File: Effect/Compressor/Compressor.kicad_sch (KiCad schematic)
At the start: 49 parts, among them J1 Conn_01x04_Pin, J2 Conn_01x04_Pin, Q1 DMMT5551, Q2 MMBF5103, Q3 DMMT5551, Q4 MMBF5103

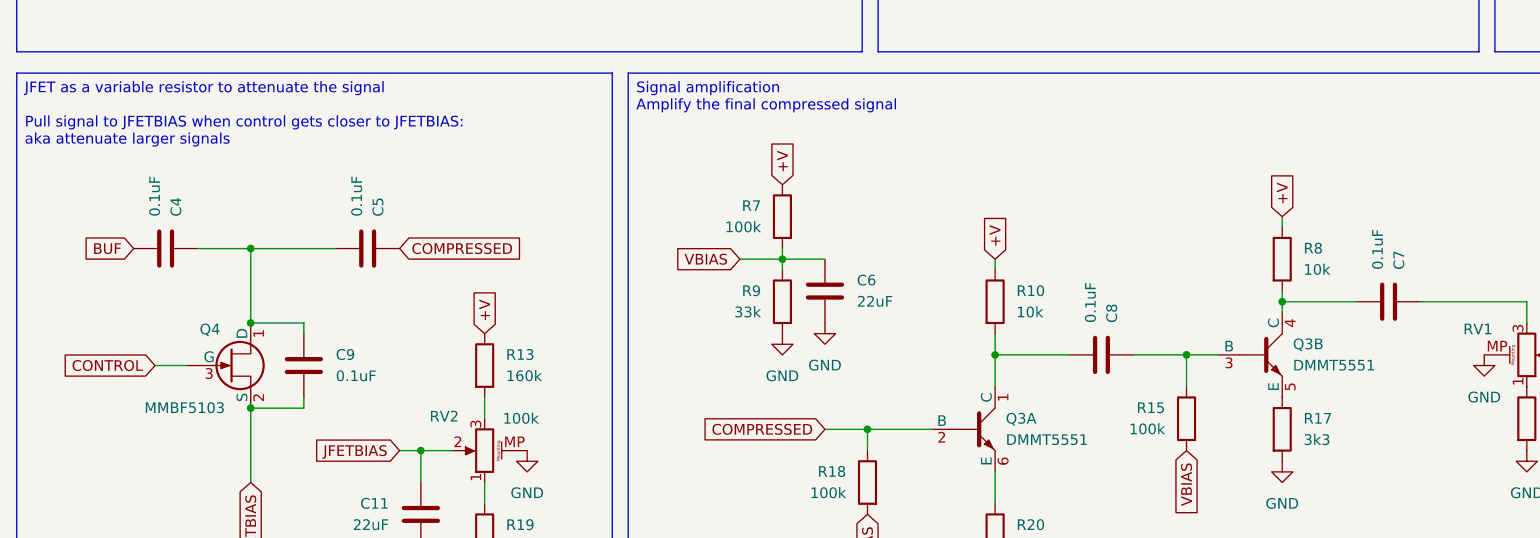
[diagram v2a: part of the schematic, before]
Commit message: Compressor: Use bigger capacitors in signal path
This just changes the 0.1uF caps in the signal path to 0.47uF ones.
That doesn't fix all ills, but it should pass lower frequency signals a
bit better.

This does make them 1206 footprints, and maybe the board will be a bit
tight.  I'm starting to look at the PCB next.

Signed-off-by: Linus Torvalds <torvalds@linux-foundation.org>
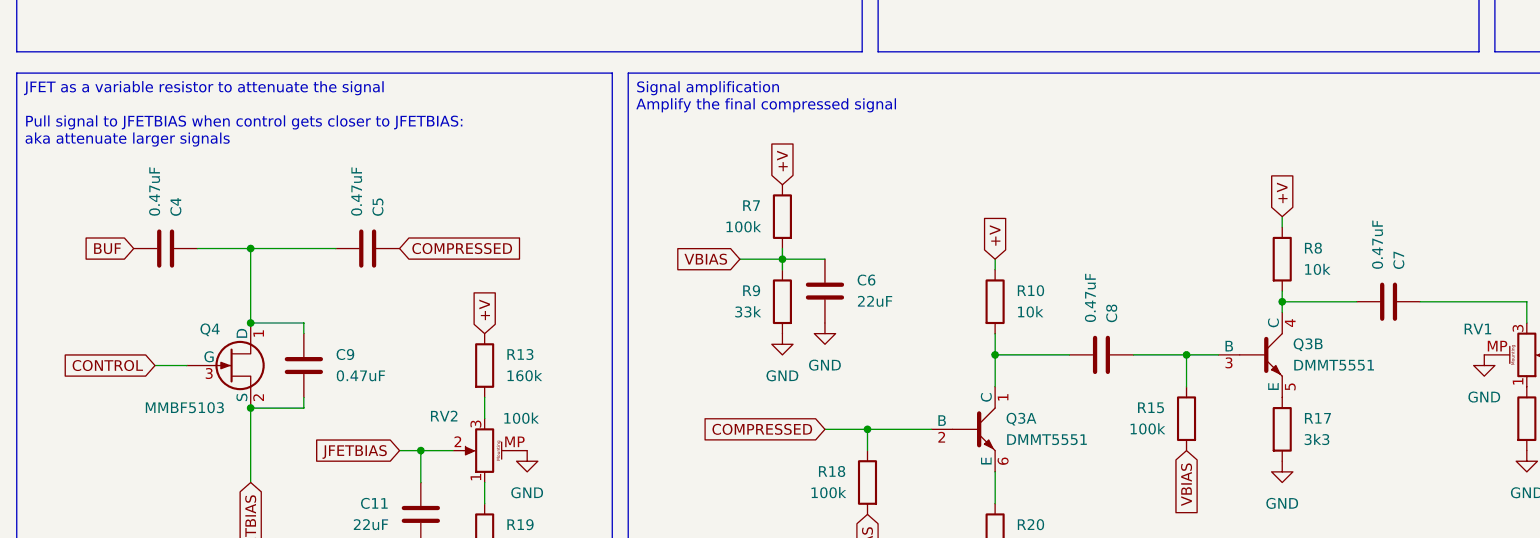
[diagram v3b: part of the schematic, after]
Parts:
- C4, C5, C7, C8, C9: value 0.1uF -> 0.47uF; footprint Mylib:C_0704_1810Metric -> Capacitor_SMD:C_1206_3216Metric
- V4: now left out of the parts list
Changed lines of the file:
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@@
 			)
 		)
-		(property "Value" "0.1uF"
+		(property "Value" "0.47uF"
 			(at 54.6101 90.17 0)
 			(effects
@@
 			)
 		)
-		(property "Footprint" "Mylib:C_0704_1810Metric"
+		(property "Footprint" "Capacitor_SMD:C_1206_3216Metric"
 			(at 52.07 93.0148 0)
 			(hide yes)
@@
 			)
 		)
-		(property "Value" "0.1uF"
+		(property "Value" "0.47uF"
 			(at 142.2401 102.87 0)
 			(effects
@@
 			)
 		)
-		(property "Footprint" "Mylib:C_0704_1810Metric"
+		(property "Footprint" "Capacitor_SMD:C_1206_3216Metric"
 			(at 139.7 105.7148 0)
 			(hide yes)
@@
 			)
 		)
-		(property "Value" "0.1uF"
+		(property "Value" "0.47uF"
 			(at 52.07 109.2199 0)
 			(effects
@@
 			)
 		)
-		(property "Footprint" "Mylib:C_0704_1810Metric"
+		(property "Footprint" "Capacitor_SMD:C_1206_3216Metric"
 			(at 49.2252 111.76 0)
 			(hide yes)
@@
 			)
 		)
-		(property "Value" "0.1uF"
+		(property "Value" "0.47uF"
 			(at 176.5301 96.52 0)
 			(effects
@@
 			)
 		)
-		(property "Footprint" "Mylib:C_0704_1810Metric"
+		(property "Footprint" "Capacitor_SMD:C_1206_3216Metric"
 			(at 173.99 99.3648 0)
 			(hide yes)
@@
 		(unit 1)
 		(exclude_from_sim no)
-		(in_bom yes)
-		(on_board yes)
+		(in_bom no)
+		(on_board no)
 		(dnp no)
 		(fields_autoplaced yes)
@@
 			)
 		)
-		(property "Value" "0.1uF"
+		(property "Value" "0.47uF"
 			(at 30.4801 90.17 0)
 			(effects
@@
 			)
 		)
-		(property "Footprint" "Mylib:C_0704_1810Metric"
+		(property "Footprint" "Capacitor_SMD:C_1206_3216Metric"
 			(at 27.94 93.0148 0)
 			(hide yes)

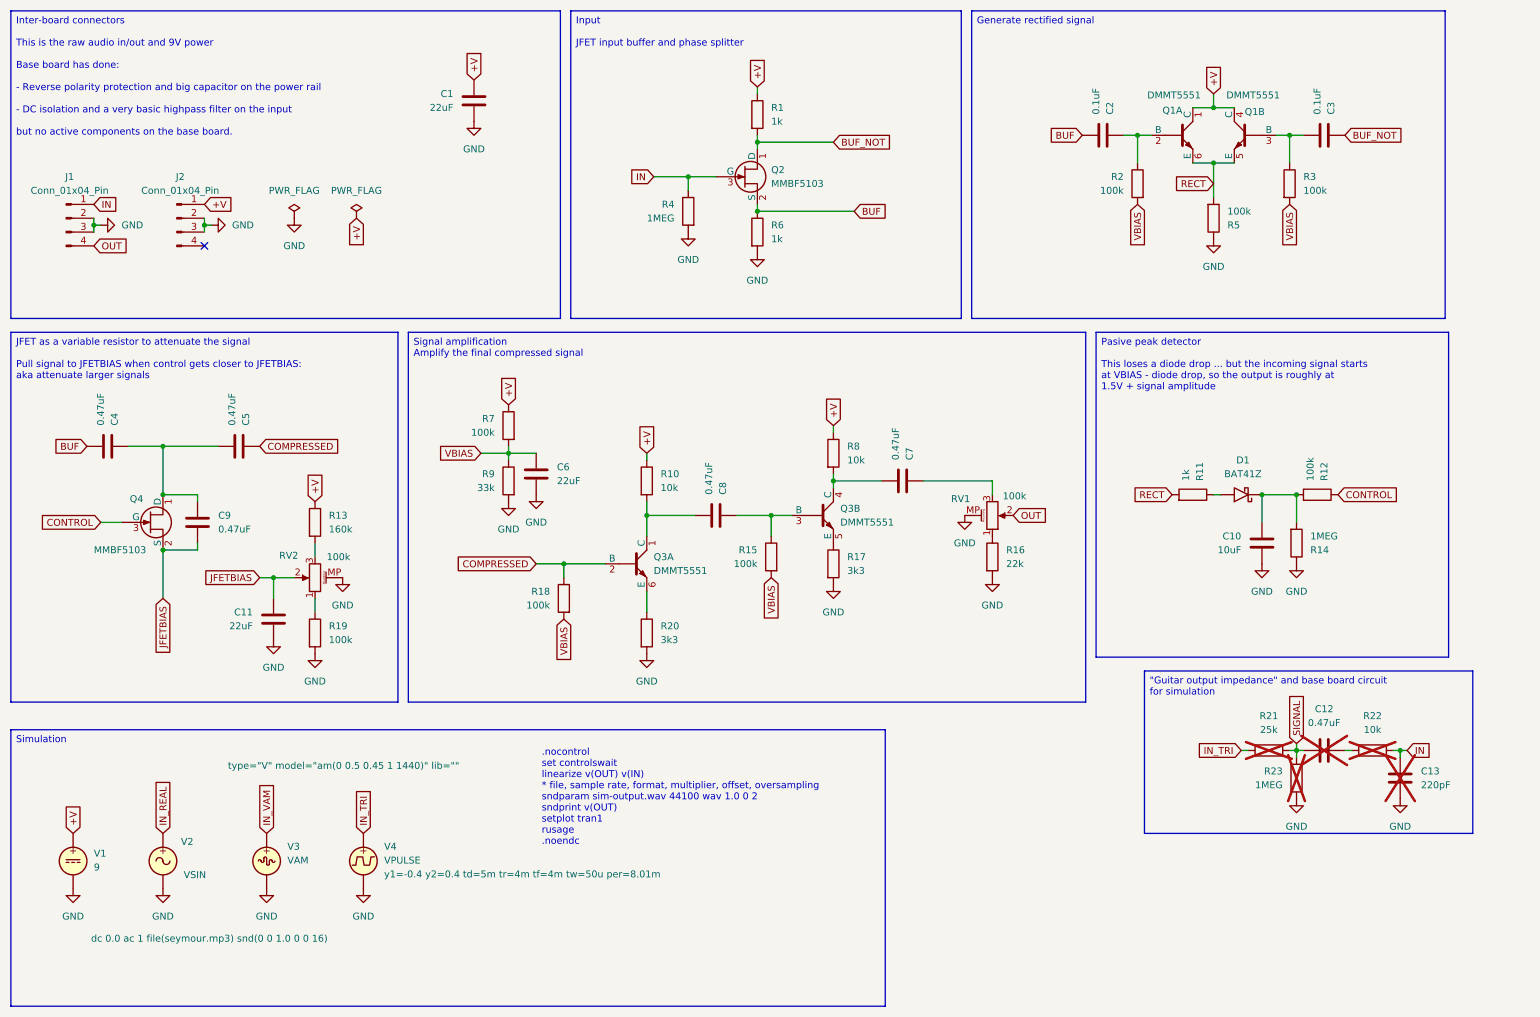
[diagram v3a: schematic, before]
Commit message: Compressor: re-do with feedback loop and a whole new approach
So as mentioned earlier I started looking into using a feedback loop
rather than base the compression purely on the input signal amplitude,
and as I was working on that, I realized that I had been thinking of the
JFET signal attenuation entirely the wrong way the whole time.

My confusion actually started way back with the old tremolo circuit that
I had so many problems with, and it all stems from just thinking that I
should use the JFET as a variable resistor to pull the signal down to
ground.

Yeah, yeah, that makes conceptual sense, but it's actually not the right
way to go about this all, because I realized that I was just making
things much harder than they needed to be.

It's much simpler and more practical to use a regular fixed resistor to
attenuate the signal by pulling it down to ground, and use the JFET to
actually _pass_ the signal.  After all, the default for the JFET is to
conduct, and R_{DS(ON)} is some reasonably small value like 50 Ohm.

So just turn things around, and it all becomes much more natural: with a
regular pull-down resistor in the kOhm range, the "normal" situation
(the JFET gate not actively pulled down) being that the JFET conducts
the signal and there is little to no attenuation.

Then when we want to attenuate the signal, we pull the gate down, and it
turns out that there's a very natural way to generate a negative signal
even without a dual power rail: just amplify the signal to have a large
enough voltage swing, and then do just a "voltage doubler" with two
capacitors and diodes.

It's just an inverting charge pump on the signal, in other words.  And
since it goes to the gate of the JFET, there's no need for any current.

Ta-daa, you have a nice negative voltage matching the signal amplitude
(with two diode drops, but just use a low-drop Schottky to minimize that
too).

And now the "add in half the input signal to the control signal" that I
had seen mentioned in JFET com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
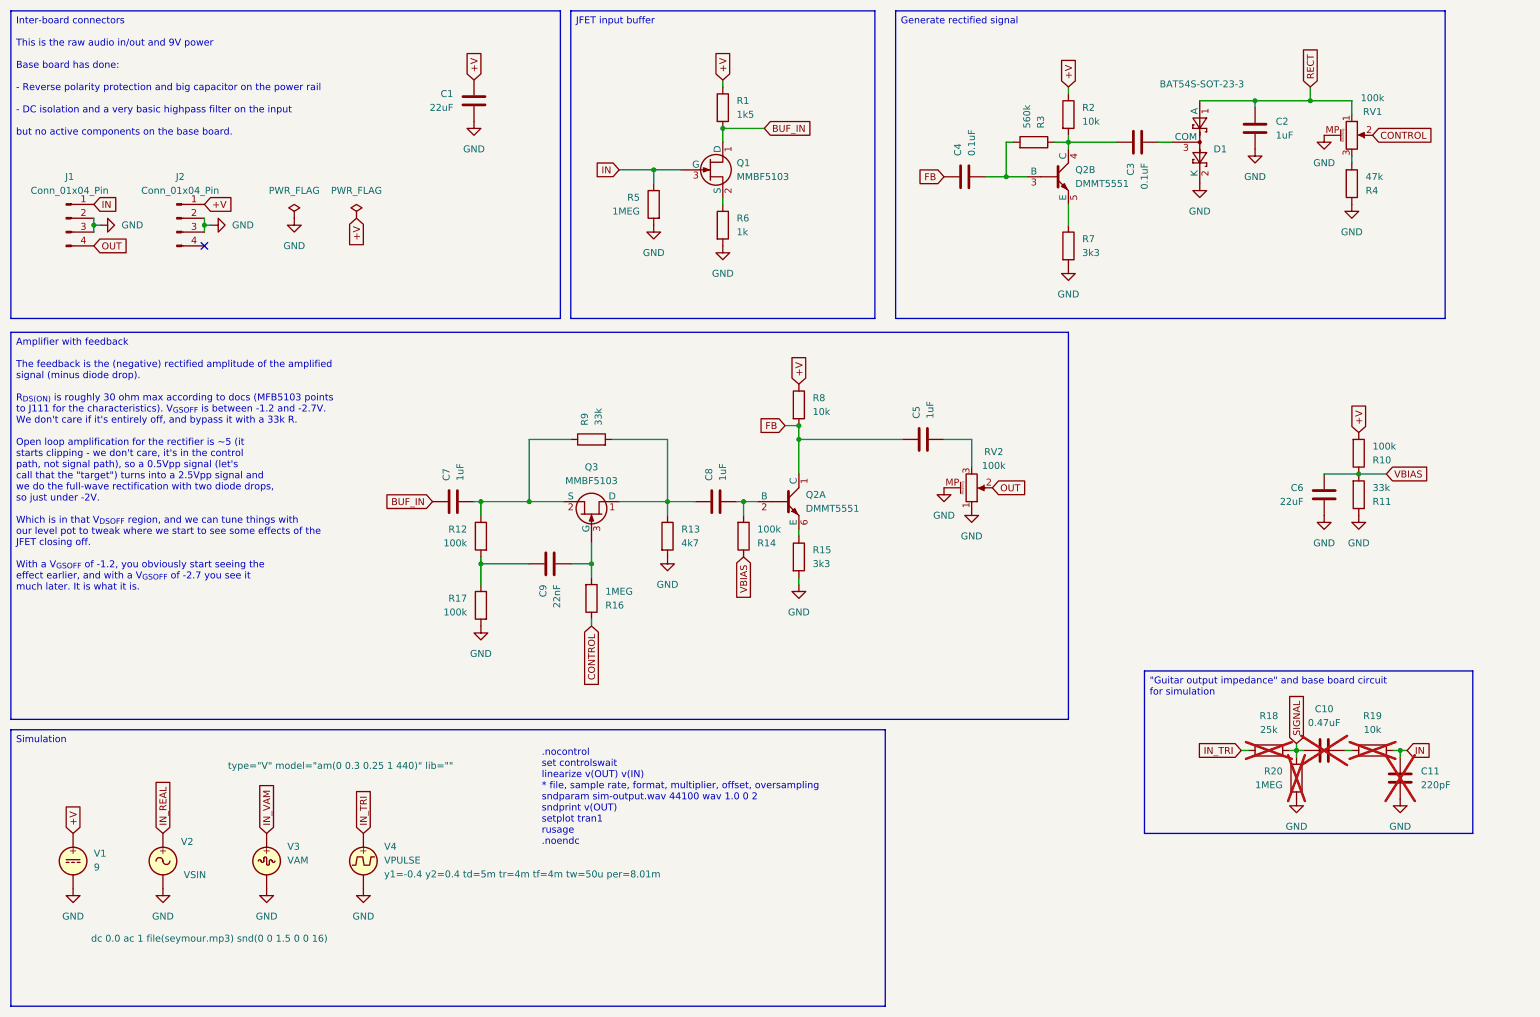
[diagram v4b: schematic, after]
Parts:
- removed C10: 10uF, Capacitor_SMD:C_1206_3216Metric, symbol Device:C
- removed C11: 22uF, Capacitor_SMD:C_1206_3216Metric, symbol Device:C
- removed D1: BAT41Z, Diode_SMD:D_SOD-123, symbol Mylib:BAT41ZFILM
- removed Q1, Q3: DMMT5551, Package_TO_SOT_SMD:SOT-23-6, symbol Mylib:DMMT5551
- removed Q4: MMBF5103, Package_TO_SOT_SMD:SOT-23, symbol Mylib:MMBF5103
- removed R18, R19, R5: 100k, Resistor_SMD:R_0805_2012Metric, symbol Device:R
- removed R20: 3k3, Resistor_SMD:R_0805_2012Metric, symbol Device:R
- added D1: BAT54S-SOT-23-3, Package_TO_SOT_SMD:SOT-23, symbol Mylib:BAT54S-SOT-23-3
- added Q2: DMMT5551, Package_TO_SOT_SMD:SOT-23-6, symbol Mylib:DMMT5551
- added Q3: MMBF5103, Package_TO_SOT_SMD:SOT-23, symbol Mylib:MMBF5103
- added R4: 47k, Resistor_SMD:R_0805_2012Metric, symbol Device:R
- C2: value 0.1uF -> 1uF; footprint Mylib:C_0704_1810Metric -> Capacitor_SMD:C_1206_3216Metric
- C3: footprint Mylib:C_0704_1810Metric -> Capacitor_SMD:C_1206_3216Metric
- C4: value 0.47uF -> 0.1uF
- C5, C7, C8: value 0.47uF -> 1uF
- C9: value 0.47uF -> 22nF
- R1: value 1k -> 1k5
- R10: value 10k -> 100k
- R11: value 1k -> 33k
- R13: value 160k -> 4k7
- R14: value 1MEG -> 100k
- R15, R7: value 100k -> 3k3
- R16: value 22k -> 1MEG
- R17: value 3k3 -> 100k
- R2: value 100k -> 10k
- R3: value 100k -> 560k
- renumbered C12 to C10, C13 to C11, Q2 to Q1, R21 to R18, R22 to R19, R23 to R20, R4 to R5
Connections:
- net +V: now also R10.2, R2.1; no longer R10.1, R13.1, R7.1
- net CONTROL: now also R16.1, RV1.2; no longer R12.1
- net GND: now also C2.2, R11.1, R13.2, R15.2, R7.2, RV2.1, D1.2 (K), R4.1; no longer R14.1, R16.2, R9.2
- net OUT: now also RV2.2; no longer RV1.2
- net RECT: now also C2.1, RV1.1, D1.1 (A); no longer R11.2
- net VBIAS: now also R10.1, R11.2, R14.1; no longer R15.2, R2.2, R3.2, R7.2, R9.1
- net at C8.2: now also R14.2, Q2.2 (B); no longer R10.2
- net at C8.1: now also R13.1, R9.2, Q3.1 (D); no longer R15.1
- net at R12.2: now also C9.1, R17.1; no longer R14.2
- net at C7.2: now also R12.1, R9.1, Q3.2 (S); no longer R8.2
- net at RV2.3: now also C5.2; no longer R13.2
- net at RV1.3: now also R4.2; no longer C7.1
- net at R3.1: now also C3.1, R2.2, Q2.4 (C); no longer C3.2
- net BUF: no longer names the net of Q1.2 (S), R6.1
- net BUF: no longer C2.2, C4.2
- net BUF_NOT renamed BUF_IN
- net BUF_IN: now also C7.1; no longer C3.1
- net COMPRESSED renamed FB
- net FB: now also C4.1, R8.2, Q2.1 (C)
- net JFETBIAS: no longer names the net of C9.2
- net JFETBIAS: now also R16.2, Q3.3 (G); no longer RV2.2
- new net: C4.2, Q2.3 (B), R3.2
- new net: Q2.5 (E), R7.1
- new net: C3.2, D1.3 (COM)
- new net: Q2.6 (E), R15.1
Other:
- moved on the sheet: Q1, R5, R6, RV2

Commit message: Compressor: do PCB layout for the new design
As expected, this was much easier due to the simpler schematic for the
much more straightforward design.

Signed-off-by: Linus Torvalds <torvalds@linux-foundation.org>
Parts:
- C3, C4: footprint Capacitor_SMD:C_1206_3216Metric -> Mylib:C_0704_1810Metric
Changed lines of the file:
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@@
 			)
 		)
-		(property "Footprint" "Capacitor_SMD:C_1206_3216Metric"
+		(property "Footprint" "Mylib:C_0704_1810Metric"
 			(at 224.79 39.0652 0)
 			(hide yes)
@@
 			)
 		)
-		(property "Footprint" "Capacitor_SMD:C_1206_3216Metric"
+		(property "Footprint" "Mylib:C_0704_1810Metric"
 			(at 193.04 43.4848 0)
 			(hide yes)
